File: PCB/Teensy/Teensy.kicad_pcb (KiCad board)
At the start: 2 copper layers, 85.1 x 52.1 mm, 74 parts, among them IC1 CNY74-2, IC2 CNY74-2, P1 BremsOpto, Q1 IRLR2905z, Q2 IRLR2905z, Q3 IRLR2905z, Q4 IRLR2905z, Q5 IRLR2905z, U1 TEENSY_3.1+4, U2 HC_05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

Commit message: Aktuelle KiCad Daten
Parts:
- C7: value 0.1-4.7µF -> 4.7µF
- D4: value 1N4001-SMD -> 1N4001
- R24: value 1-3K -> 3K
- moved R24 3.94 mm to (164.6, 102.9)
- moved C2 0.65 mm to (166.9, 106.7)
- moved C7 0.65 mm to (164.3, 106.7)
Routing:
- net GND: track 169.9 -> 164.4 mm
- net Net-(R24-Pad1): track 8.34 -> 4.40 mm
- net +3V3: track 178.7 -> 179.2 mm

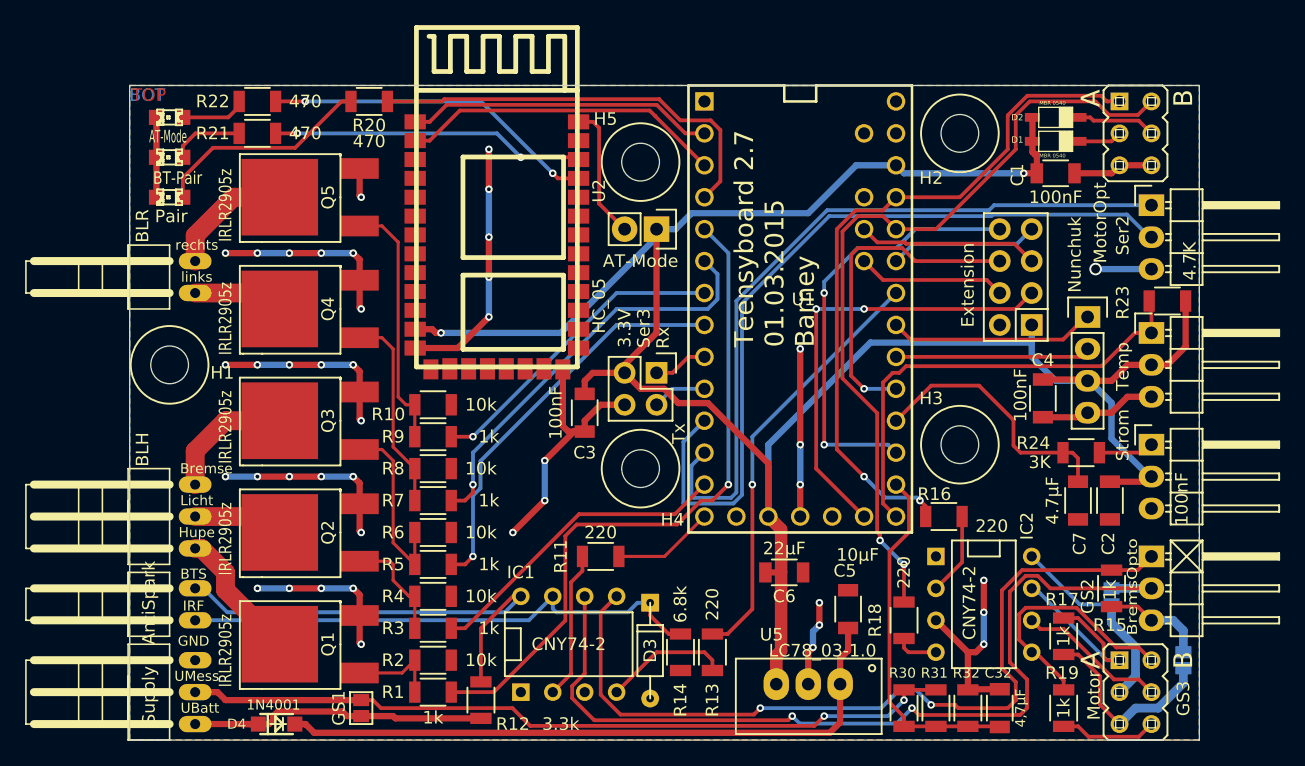
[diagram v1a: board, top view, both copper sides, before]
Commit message: Anpassungen in KiCad PCB Mount Hole hat jetzt die Bohrung 3.2mm Werte der Bauteile nicht mit "," sondern ".". Wichtig für den Export der BOM Bessere Verlegung der Spannungsmessleitung, geschützt in GND. Bohrungen auf Plausibilität geprüft. Texte auf PCB in Größe und Linienstärke gemäß Fischer Leiterplattenservice angepasst. Kupferflächen aktualisiert.
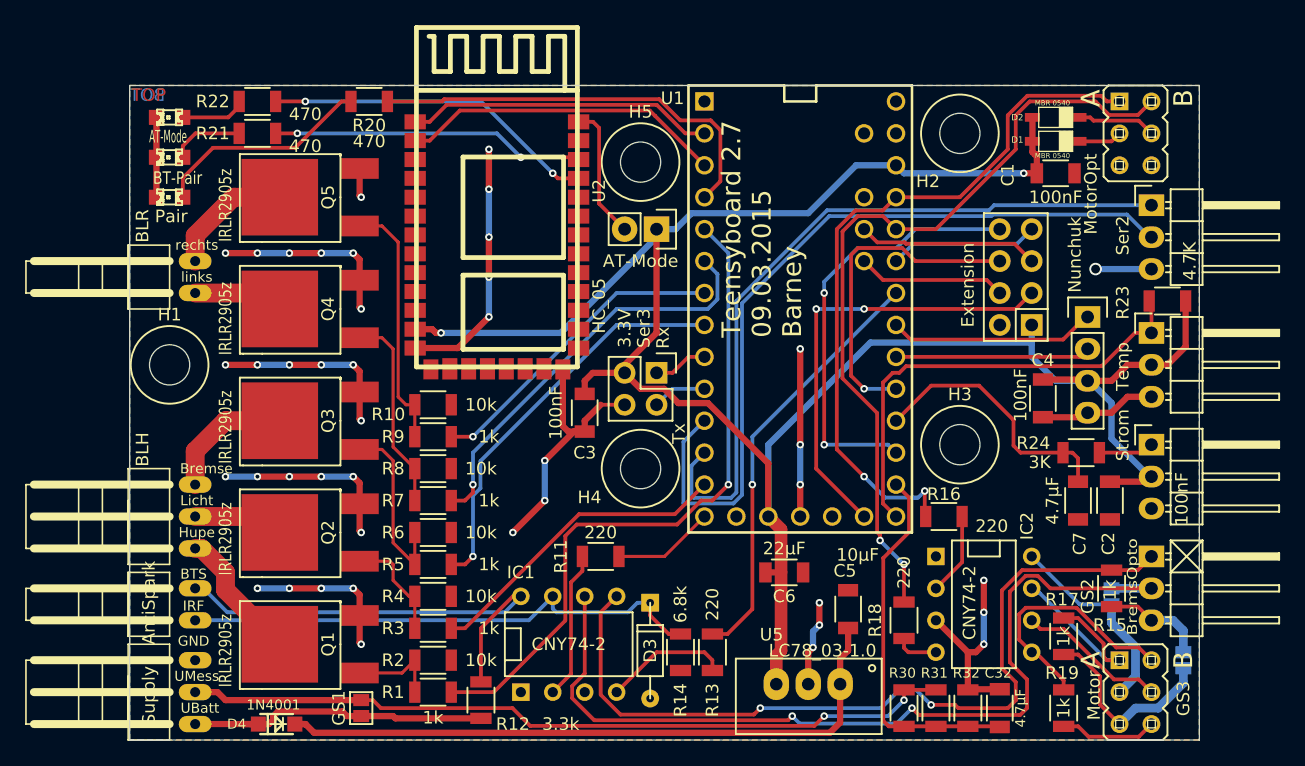
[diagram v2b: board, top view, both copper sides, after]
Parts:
- C32: value 4,7µF -> 4.7µF
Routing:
- net GND: track 164.4 -> 158.0 mm
- net Motorst_A: track 55.9 -> 57.3 mm
- net /UbMess: track 28.4 -> 29.5 mm
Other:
- board text added: "Teensyboard 2.7 09.03.2015 Barney"
- board text removed: "Teensyboard 2.7 01.03.2015 Barney"
